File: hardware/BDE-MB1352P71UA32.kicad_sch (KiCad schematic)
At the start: 11 parts, among them J401 Conn_ARM_JTAG_SWD_10, SW401 SW_Push, U401 USBLC6-2P6, U402 USBLC6-2P6, U403 BDE-MB1352P71UA32

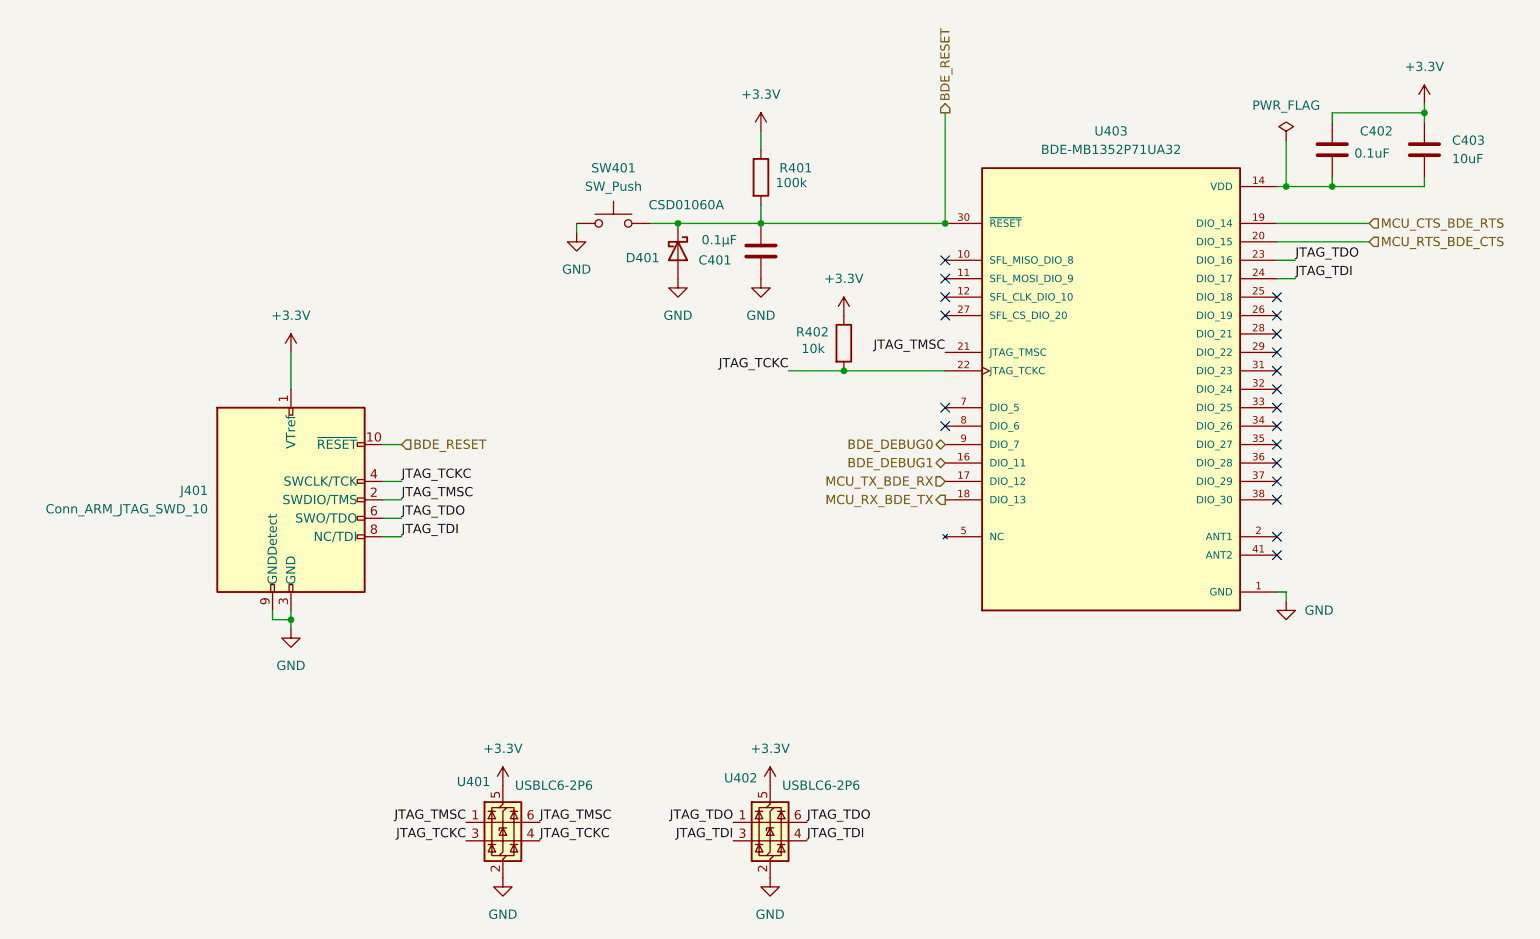
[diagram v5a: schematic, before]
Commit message: updated labels
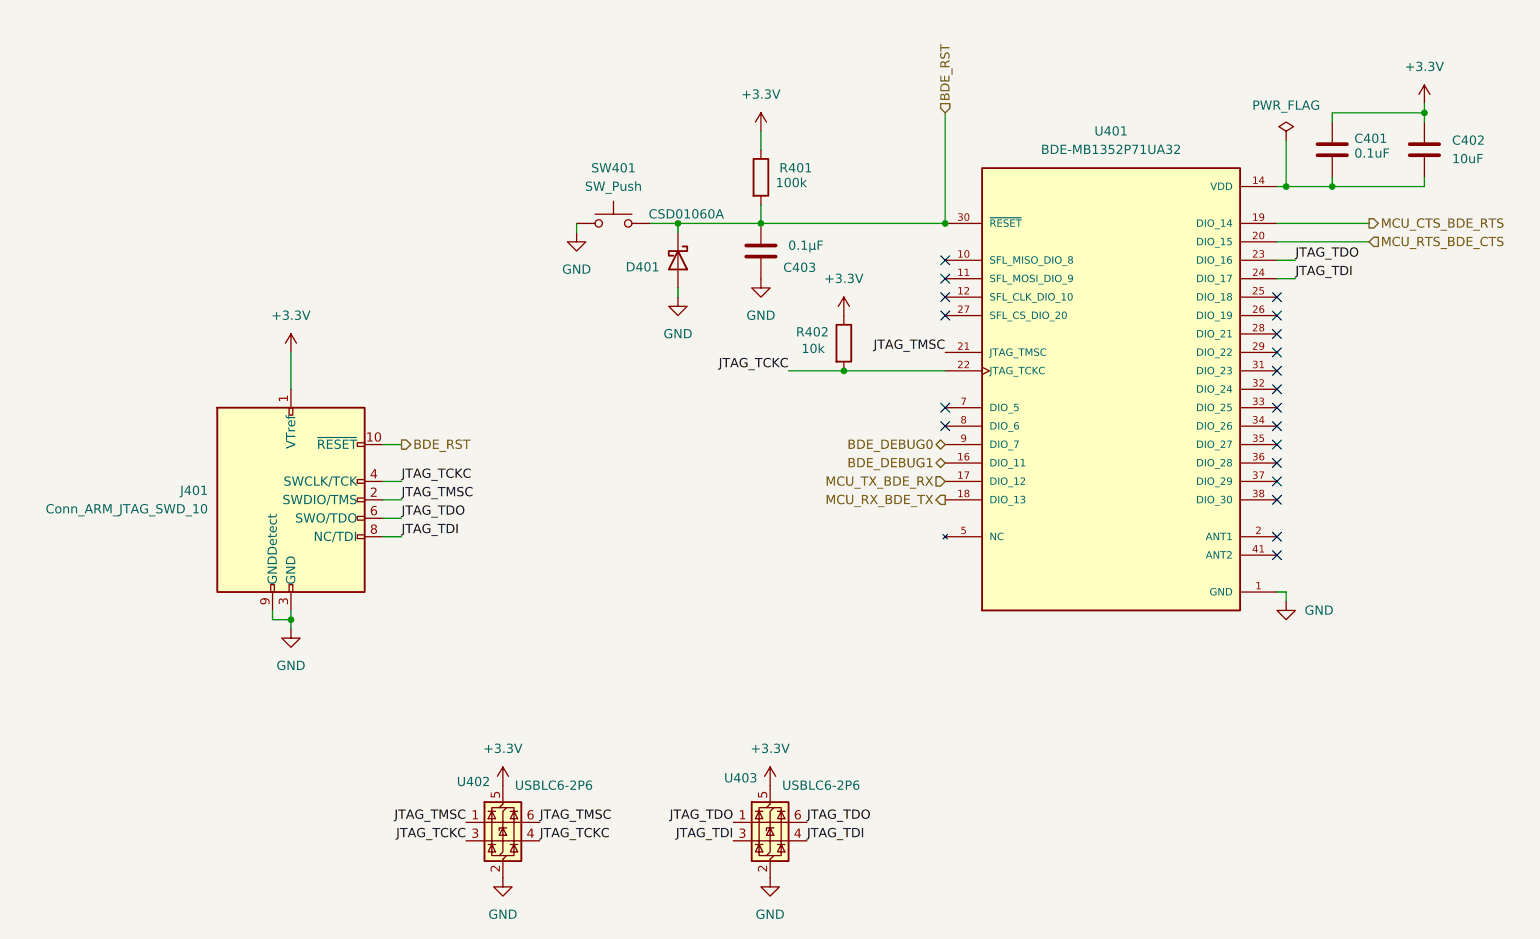
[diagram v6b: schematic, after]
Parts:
- renumbered C402 to C401, C403 to C402, C401 to C403, U403 to U401, U401 to U402, U402 to U403
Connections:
- net BDE_RESET renamed BDE_RST
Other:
- moved on the sheet: D401
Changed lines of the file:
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@@
+	(wire
+		(pts
+			(xy 129.54 63.5) (xy 129.54 62.23)
+		)
+		(stroke
+			(width 0)
+			(type default)
+		)
+	)
 	(wire
 		(pts
@@
 	(wire
 		(pts
-			(xy 144.78 82.55) (xy 152.4 82.55)
+			(xy 129.54 72.39) (xy 129.54 71.12)
 		)
 		(stroke
@@
 	(wire
 		(pts
-			(xy 88.9 102.87) (xy 91.44 102.87)
+			(xy 144.78 82.55) (xy 152.4 82.55)
 		)
 		(stroke
@@
 		)
 	)
+	(wire
+		(pts
+			(xy 88.9 102.87) (xy 91.44 102.87)
+		)
+		(stroke
+			(width 0)
+			(type default)
+		)
+	)
 	(label "JTAG_TMSC"
 		(at 91.44 100.33 0)
@@
 	)
 	(hierarchical_label "MCU_CTS_BDE_RTS"
-		(shape input)
+		(shape output)
 		(at 224.79 62.23 0)
 		(effects
@@
 		)
 	)
-	(hierarchical_label "BDE_RESET"
+	(hierarchical_label "BDE_RST"
+		(shape input)
+		(at 166.37 46.99 90)
+		(effects
+			(font
+				(size 1.27 1.27)
+			)
+			(justify left)
+		)
+	)
+	(hierarchical_label "BDE_RST"
 		(shape output)
-		(at 166.37 46.99 90)
-		(effects
-			(font
-				(size 1.27 1.27)
-			)
-			(justify left)
-		)
-	)
-	(hierarchical_label "BDE_RESET"
-		(shape input)
 		(at 91.44 92.71 0)
 		(effects
@@
 		(dnp no)
 		(fields_autoplaced yes)
-		(property "Reference" "#PWR0409"
+		(property "Reference" "#PWR0411"
 			(at 142.24 143.51 0)
 			(effects
@@
 			(project "Senior_Design"
 				(path "/8f5928e8-0fc1-4443-a20f-3bfeb956761e/dd2813e4-a810-44d7-8b7e-d46ce1c3fa30"
-					(reference "#PWR0409")
+					(reference "#PWR0411")
 					(unit 1)
 				)
@@
 		(dnp no)
 		(fields_autoplaced yes)
-		(property "Reference" "#PWR0411"
+		(property "Reference" "#PWR0406"
 			(at 152.4 78.74 0)
 			(effects
@@
 			(project "Senior_Design"
 				(path "/8f5928e8-0fc1-4443-a20f-3bfeb956761e/dd2813e4-a810-44d7-8b7e-d46ce1c3fa30"
-					(reference "#PWR0411")
+					(reference "#PWR0406")
 					(unit 1)
 				)
@@
 		(on_board yes)
 		(dnp no)
-		(property "Reference" "U402"
+		(property "Reference" "U403"
 			(at 135.89 138.684 0)
 			(effects
@@
 			(project "Senior_Design"
 				(path "/8f5928e8-0fc1-4443-a20f-3bfeb956761e/dd2813e4-a810-44d7-8b7e-d46ce1c3fa30"
-					(reference "U402")
+					(reference "U403")
 					(unit 1)
 				)
@@
 	(symbol
 		(lib_id "power:GND")
-		(at 129.54 69.85 0)
+		(at 129.54 72.39 0)
 		(unit 1)
 		(exclude_from_sim no)
@@
 		(dnp no)
 		(fields_autoplaced yes)
-		(property "Reference" "#PWR0406"
-			(at 129.54 76.2 0)
+		(property "Reference" "#PWR0405"
+			(at 129.54 78.74 0)
 			(effects
 				(font
@@
 		)
 		(property "Value" "GND"
-			(at 129.54 74.93 0)
+			(at 129.54 77.47 0)
 			(effects
 				(font
@@
 		)
 		(property "Footprint" ""
-			(at 129.54 69.85 0)
+			(at 129.54 72.39 0)
 			(effects
 				(font
@@
 		)
 		(property "Datasheet" ""
-			(at 129.54 69.85 0)
+			(at 129.54 72.39 0)
 			(effects
 				(font
@@
 		)
 		(property "Description" "Power symbol creates a global label with name \"GND\" , ground"
-			(at 129.54 69.85 0)
-			(effects
-				(font
-					(size 1.27 1.27)
-				)
-				(hide yes)
-			)
-		)
-		(pin "1"
-		)
-		(instances
-			(project "Senior_Design"
-				(path "/8f5928e8-0fc1-4443-a20f-3bfeb956761e/dd2813e4-a810-44d7-8b7e-d46ce1c3fa30"
-					(reference "#PWR0406")
+			(at 129.54 72.39 0)
+			(effects
+				(font
+					(size 1.27 1.27)
+				)
+				(hide yes)
+			)
+		)
+		(pin "1"
+		)
+		(instances
+			(project "Senior_Design"
+				(path "/8f5928e8-0fc1-4443-a20f-3bfeb956761e/dd2813e4-a810-44d7-8b7e-d46ce1c3fa30"
+					(reference "#PWR0405")
 					(unit 1)
 				)
@@
 		(on_board yes)
 		(dnp no)
-		(property "Reference" "C402"
-			(at 223.52 49.5299 0)
+		(property "Reference" "C401"
+			(at 222.758 50.546 0)
 			(effects
 				(font
@@
 			(project "Senior_Design"
 				(path "/8f5928e8-0fc1-4443-a20f-3bfeb956761e/dd2813e4-a810-44d7-8b7e-d46ce1c3fa30"
-					(reference "C402")
+					(reference "C401")
 					(unit 1)
 				)
@@
 		(on_board yes)
 		(dnp no)
-		(property "Reference" "U401"
+		(property "Reference" "U402"
 			(at 99.06 139.192 0)
 			(effects
@@
 			(project "Senior_Design"
 				(path "/8f5928e8-0fc1-4443-a20f-3bfeb956761e/dd2813e4-a810-44d7-8b7e-d46ce1c3fa30"
-					(reference "U401")
+					(reference "U402")
 					(unit 1)
 				)
@@
 		(dnp no)
 		(fields_autoplaced yes)
-		(property "Reference" "#PWR0402"
+		(property "Reference" "#PWR0409"
 			(at 76.2 124.46 0)
 			(effects
@@
 			(project "Senior_Design"
 				(path "/8f5928e8-0fc1-4443-a20f-3bfeb956761e/dd2813e4-a810-44d7-8b7e-d46ce1c3fa30"
-					(reference "#PWR0402")
+					(reference "#PWR0409")
 					(unit 1)
 				)
@@
 		(on_board yes)
 		(dnp no)
-		(property "Reference" "C401"
-			(at 136.906 67.31 0)
+		(property "Reference" "C403"
+			(at 148.59 68.326 0)
 			(effects
 				(font
@@
 		)
 		(property "Value" "0.1µF"
-			(at 137.668 64.516 0)
+			(at 149.606 65.278 0)
 			(effects
 				(font
@@
 			(project "Senior_Design"
 				(path "/8f5928e8-0fc1-4443-a20f-3bfeb956761e/dd2813e4-a810-44d7-8b7e-d46ce1c3fa30"
-					(reference "C401")
+					(reference "C403")
 					(unit 1)
 				)
@@
 		(dnp no)
 		(fields_autoplaced yes)
-		(property "Reference" "#PWR0408"
+		(property "Reference" "#PWR0404"
 			(at 140.97 76.2 0)
 			(effects
@@
 			(project "Senior_Design"
 				(path "/8f5928e8-0fc1-4443-a20f-3bfeb956761e/dd2813e4-a810-44d7-8b7e-d46ce1c3fa30"
-					(reference "#PWR0408")
+					(reference "#PWR0404")
 					(unit 1)
 				)
@@
 		(dnp no)
 		(fields_autoplaced yes)
-		(property "Reference" "#PWR0403"
+		(property "Reference" "#PWR0410"
 			(at 105.41 143.51 0)
 			(effects
@@
 			(project "Senior_Design"
 				(path "/8f5928e8-0fc1-4443-a20f-3bfeb956761e/dd2813e4-a810-44d7-8b7e-d46ce1c3fa30"
-					(reference "#PWR0403")
+					(reference "#PWR0410")
 					(unit 1)
 				)
@@
 		(dnp no)
 		(fields_autoplaced yes)
-		(property "Reference" "U403"
+		(property "Reference" "U401"
 			(at 189.23 49.53 0)
 			(effects
@@
 			(project "Senior_Design"
 				(path "/8f5928e8-0fc1-4443-a20f-3bfeb956761e/dd2813e4-a810-44d7-8b7e-d46ce1c3fa30"
-					(reference "U403")
+					(reference "U401")
 					(unit 1)
 				)
@@
 		(dnp no)
 		(fields_autoplaced yes)
-		(property "Reference" "#PWR0407"
+		(property "Reference" "#PWR0402"
 			(at 140.97 53.34 0)
 			(effects
@@
 			(project "Senior_Design"
 				(path "/8f5928e8-0fc1-4443-a20f-3bfeb956761e/dd2813e4-a810-44d7-8b7e-d46ce1c3fa30"
-					(reference "#PWR0407")
+					(reference "#PWR0402")
 					(unit 1)
 				)
@@
 		(dnp no)
 		(fields_autoplaced yes)
-		(property "Reference" "#PWR0401"
+		(property "Reference" "#PWR0407"
 			(at 76.2 83.82 0)
 			(effects
@@
 			(project "Senior_Design"
 				(path "/8f5928e8-0fc1-4443-a20f-3bfeb956761e/dd2813e4-a810-44d7-8b7e-d46ce1c3fa30"
-					(reference "#PWR0401")
+					(reference "#PWR0407")
 					(unit 1)
 				)
@@
 	(symbol
 		(lib_id "Diode:CSD01060A")
-		(at 129.54 66.04 270)
+		(at 129.54 67.31 270)
 		(unit 1)
 		(exclude_from_sim no)
@@
 		(dnp no)
 		(property "Reference" "D401"
-			(at 127 66.9926 90)
+			(at 127 68.2626 90)
 			(effects
 				(font
@@
 		)
 		(property "Value" "CSD01060A"
-			(at 135.89 59.69 90)
+			(at 135.89 60.96 90)
 			(effects
 				(font
@@
 		)
 		(property "Footprint" "Diode_SMD:D_SOD-123"
-			(at 125.095 66.04 0)
+			(at 125.095 67.31 0)
 			(effects
 				(font
@@
 		)
 		(property "Datasheet" "https://www.wolfspeed.com/media/downloads/87/CSD01060.pdf"
-			(at 129.54 66.04 0)
+			(at 129.54 67.31 0)
 			(effects
 				(font
@@
 		)
 		(property "Description" "600V, 1A, SiC Schottky Diode, TO-220"
-			(at 129.54 66.04 0)
+			(at 129.54 67.31 0)
 			(effects
 				(font
@@
 		(dnp no)
 		(fields_autoplaced yes)
-		(property "Reference" "#PWR0412"
+		(property "Reference" "#PWR0408"
 			(at 213.36 120.65 0)
 			(effects
@@
 			(project "Senior_Design"
 				(path "/8f5928e8-0fc1-4443-a20f-3bfeb956761e/dd2813e4-a810-44d7-8b7e-d46ce1c3fa30"
-					(reference "#PWR0412")
+					(reference "#PWR0408")
 					(unit 1)
 				)
@@
 		(dnp no)
 		(fields_autoplaced yes)
-		(property "Reference" "#PWR0405"
+		(property "Reference" "#PWR0403"
 			(at 115.57 69.85 0)
 			(effects
@@
 			(project "Senior_Design"
 				(path "/8f5928e8-0fc1-4443-a20f-3bfeb956761e/dd2813e4-a810-44d7-8b7e-d46ce1c3fa30"
-					(reference "#PWR0405")
+					(reference "#PWR0403")
 					(unit 1)
 				)
@@
 		(dnp no)
 		(fields_autoplaced yes)
-		(property "Reference" "C403"
+		(property "Reference" "C402"
 			(at 236.22 50.7999 0)
 			(effects
@@
 			(project "Senior_Design"
 				(path "/8f5928e8-0fc1-4443-a20f-3bfeb956761e/dd2813e4-a810-44d7-8b7e-d46ce1c3fa30"
-					(reference "C403")
+					(reference "C402")
 					(unit 1)
 				)
@@
 		(dnp no)
 		(fields_autoplaced yes)
-		(property "Reference" "#PWR0404"
+		(property "Reference" "#PWR0412"
 			(at 105.41 158.75 0)
 			(effects
@@
 			(project "Senior_Design"
 				(path "/8f5928e8-0fc1-4443-a20f-3bfeb956761e/dd2813e4-a810-44d7-8b7e-d46ce1c3fa30"
-					(reference "#PWR0404")
+					(reference "#PWR0412")
 					(unit 1)
 				)
@@
 		(dnp no)
 		(fields_autoplaced yes)
-		(property "Reference" "#PWR0410"
+		(property "Reference" "#PWR0413"
 			(at 142.24 158.75 0)
 			(effects
@@
 			(project "Senior_Design"
 				(path "/8f5928e8-0fc1-4443-a20f-3bfeb956761e/dd2813e4-a810-44d7-8b7e-d46ce1c3fa30"
-					(reference "#PWR0410")
+					(reference "#PWR0413")
 					(unit 1)
 				)
@@
 		(dnp no)
 		(fields_autoplaced yes)
-		(property "Reference" "#PWR0413"
+		(property "Reference" "#PWR0401"
 			(at 232.41 49.53 0)
 			(effects
@@
 			(project "Senior_Design"
 				(path "/8f5928e8-0fc1-4443-a20f-3bfeb956761e/dd2813e4-a810-44d7-8b7e-d46ce1c3fa30"
-					(reference "#PWR0413")
-					(unit 1)
-				)
+					(reference "#PWR0401")
+					(unit 1)
+				)
